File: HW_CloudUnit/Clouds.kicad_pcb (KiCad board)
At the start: 2 copper layers, 21.6 x 27 mm, 30 parts, among them J1 Conn_01x06, J2 Conn_01x03, J3 Conn_01x04, J4 Conn_01x04, U1 STM32G030F6Px, U2 AS5600L-ASOM, U3 DRV8313PWPR

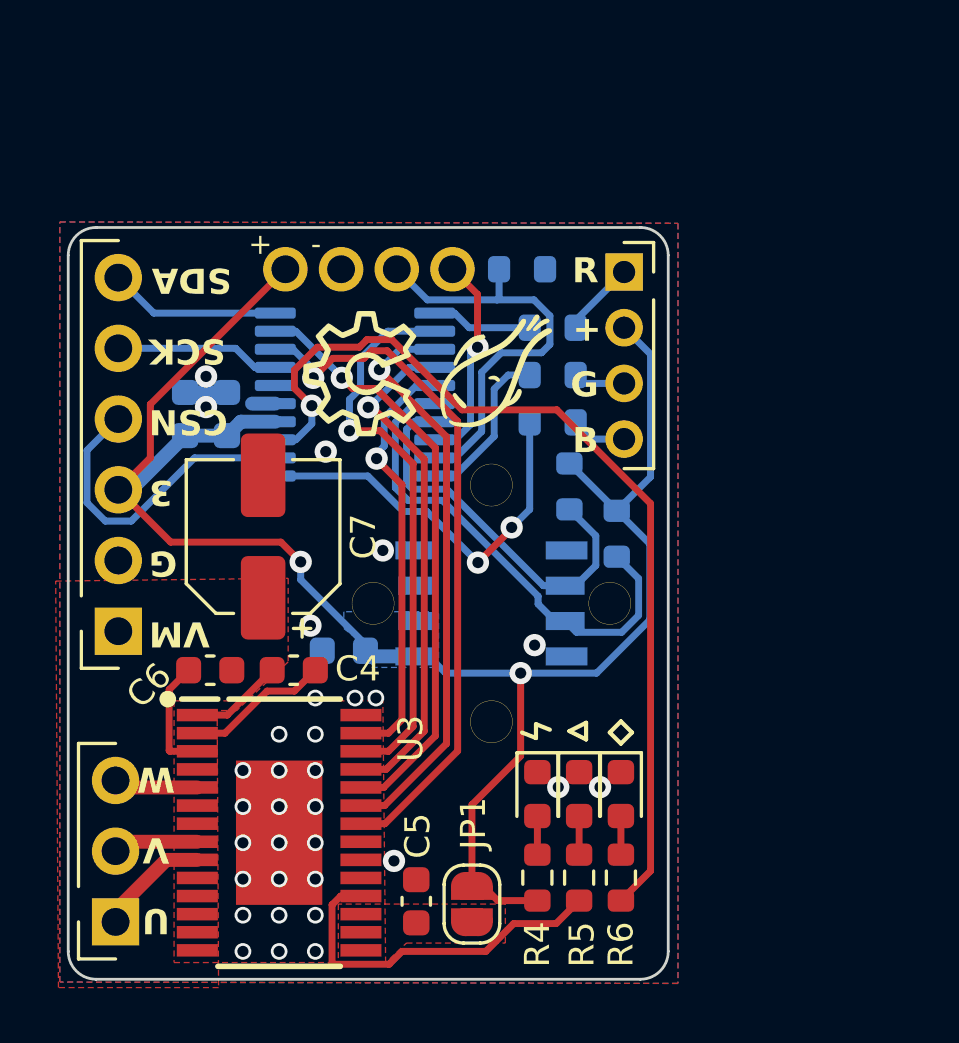
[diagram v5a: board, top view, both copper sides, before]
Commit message: Update clouds unit PCB with new motor dimensions
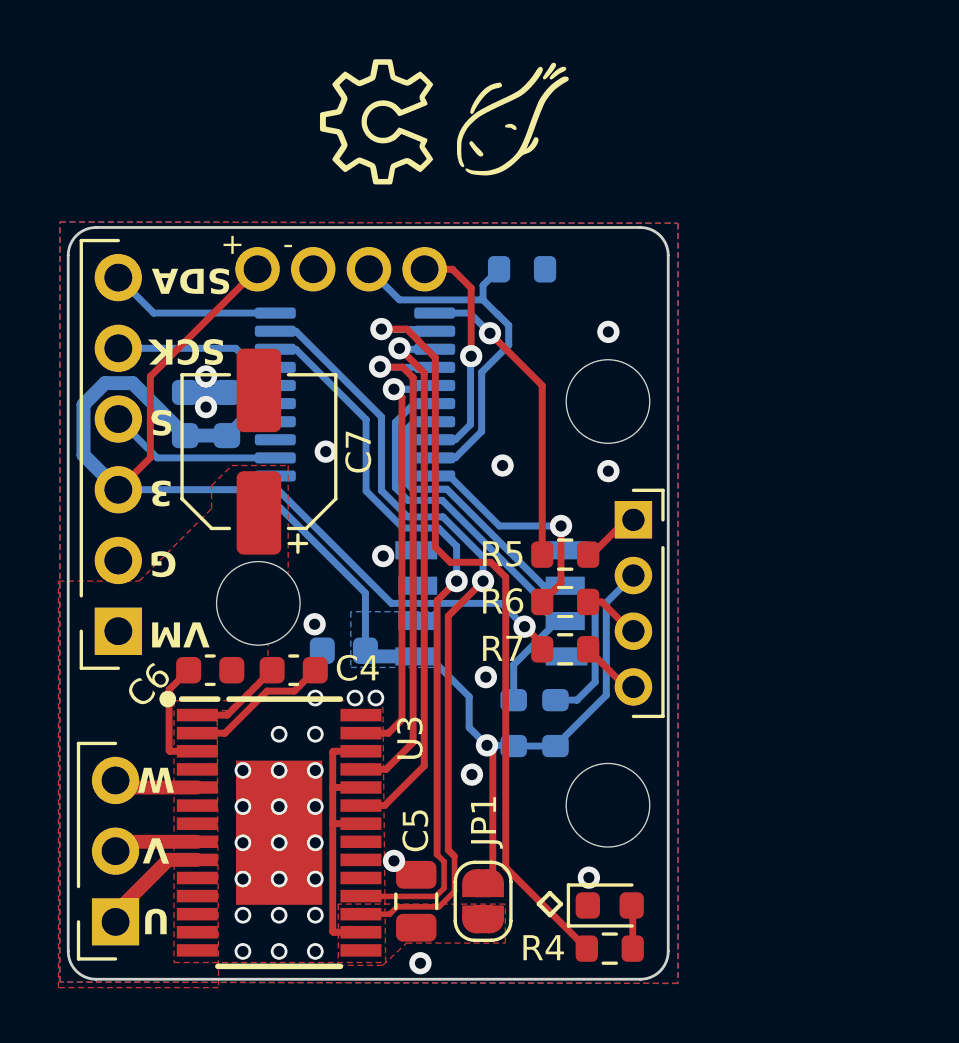
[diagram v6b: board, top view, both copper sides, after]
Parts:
- removed the D1 at (35.0, 38.5)
- removed D2: Green, LED_SMD:LED_0603_1608Metric
- removed the R4 at (35.0, 41.5)
- removed the R5 at (36.5, 41.5)
- C5: footprint Capacitor_SMD:C_0603_1608Metric -> Capacitor_SMD:C_0805_2012Metric
- H1: footprint Clouds_footprints:MountingHoles_M1.4_Diag8.5 -> Clouds_footprints:MountingHoles_M3_Tri14.5
- R5: renamed from R7; value TBD -> 220; moved to F.Cu
- R6: renamed from R8; value TBD -> 220; moved to F.Cu
- R7: renamed from R9; value TBD -> 220; moved to F.Cu
- moved G*** 9.06 mm to (34.2, 14.2)
- moved G*** 9.06 mm to (29.3, 14.4)
- moved J3 8.91 mm to (38.5, 28.7)
- moved R3 8.51 mm to (35.7, 36.0), turned to 90 degrees
- moved R7 8.16 mm to (36.0, 33.4)
- moved R5 8.16 mm to (36.0, 29.9)
- moved R6 8.16 mm to (36.0, 31.6)
- moved R2 7.74 mm to (34.2, 36.0), turned to 90 degrees
- moved D1 4.02 mm to (37.6, 42.5), turned to 0 degrees
- moved C7 3.05 mm to (25.1, 26.2)
- moved R4 2.58 mm to (37.6, 44.1), turned to 0 degrees
- moved J4 1.00 mm to (28.0, 19.7)
- moved JP1 0.41 mm to (33.1, 42.4)
- turned H1 to -30 degrees
- renumbered D3 to D1, R6 to R4
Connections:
- U1 pad 12: EN_W -> LED_ACT
- U1 pad 3: LED_ACT -> unconnected-(U1-PC15-Pad3)
- U1 pad 8: EN_U -> NFAULT
- U1 pad 9: EN_V -> NSLEEP
- U3 pad 17: V3P3O -> NSLEEP
- U3 pad 22: EN_U -> V3P3O
- U3 pad 24: EN_V -> V3P3O
- U3 pad 26: EN_W -> V3P3O
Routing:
- net NSLEEP: track 0.00 -> 28.7 mm, vias 0 -> 1
- net EN_U: track 25.0 -> 0.00 mm, vias 1 -> 0
- net EN_V: track 21.3 -> 0.00 mm, vias 1 -> 0
- net EN_W: track 20.3 -> 0.00 mm, vias 1 -> 0
- net NFAULT: track 13.1 -> 26.7 mm, vias 0 -> 1
- net V3P3O: track 0.00 -> 10.5 mm
- net +3.3V: track 65.1 -> 55.8 mm, vias 2 -> 1
- net LED_R: track 3.63 -> 11.0 mm, vias 0 -> 1
- net LED_ACT: track 34.1 -> 28.6 mm
- net UNIT_CSN: track 11.4 -> 6.22 mm
- net LED_G: track 5.91 -> 8.29 mm, vias 0 -> 1
- net MAG_SDA: track 14.6 -> 16.6 mm
- net SWCLK: track 15.4 -> 13.5 mm
- net LED_B: track 14.4 -> 12.5 mm, vias 2 -> 1
- net Net-(D2-A): track 1.39 -> 0.00 mm
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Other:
- board text added: "S"
- board text removed: "+"
- board text removed: "B"
- board text removed: "CSN"
- board text removed: "R"

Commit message: Further revise PCB design
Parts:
- moved G*** 12.3 mm to (33.8, 25.9)
- moved G*** 6.70 mm to (33.6, 20.9)
- moved C6 3.07 mm to (20.4, 35.0), turned to 180 degrees
- moved C4 2.85 mm to (23.4, 34.2)
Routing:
- net Net-(U3-CPH): track 5.18 -> 3.24 mm
- net Net-(U3-CPL): track 3.36 -> 1.58 mm
- net +3.3V: track 55.8 -> 54.6 mm
- net Net-(U3-VCP): track 4.20 -> 3.28 mm
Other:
- board text added: "23-WnSolst"
- board text added: "Rev. 4"
- board text removed: "*"
- board text removed: "23-Flurry"
- board text removed: "Rev. 3"

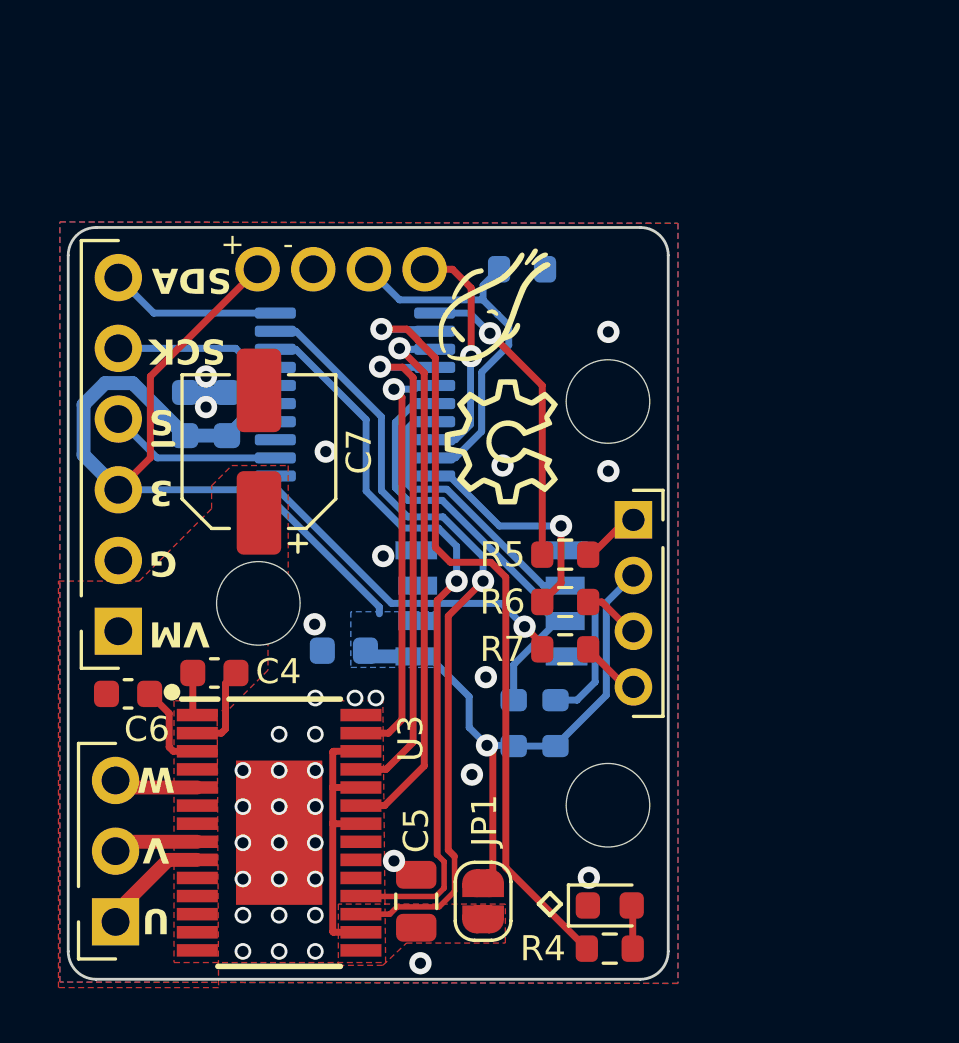
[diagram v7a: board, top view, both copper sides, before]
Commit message: Revise PCB and submit for fabrication (Rev. 4)
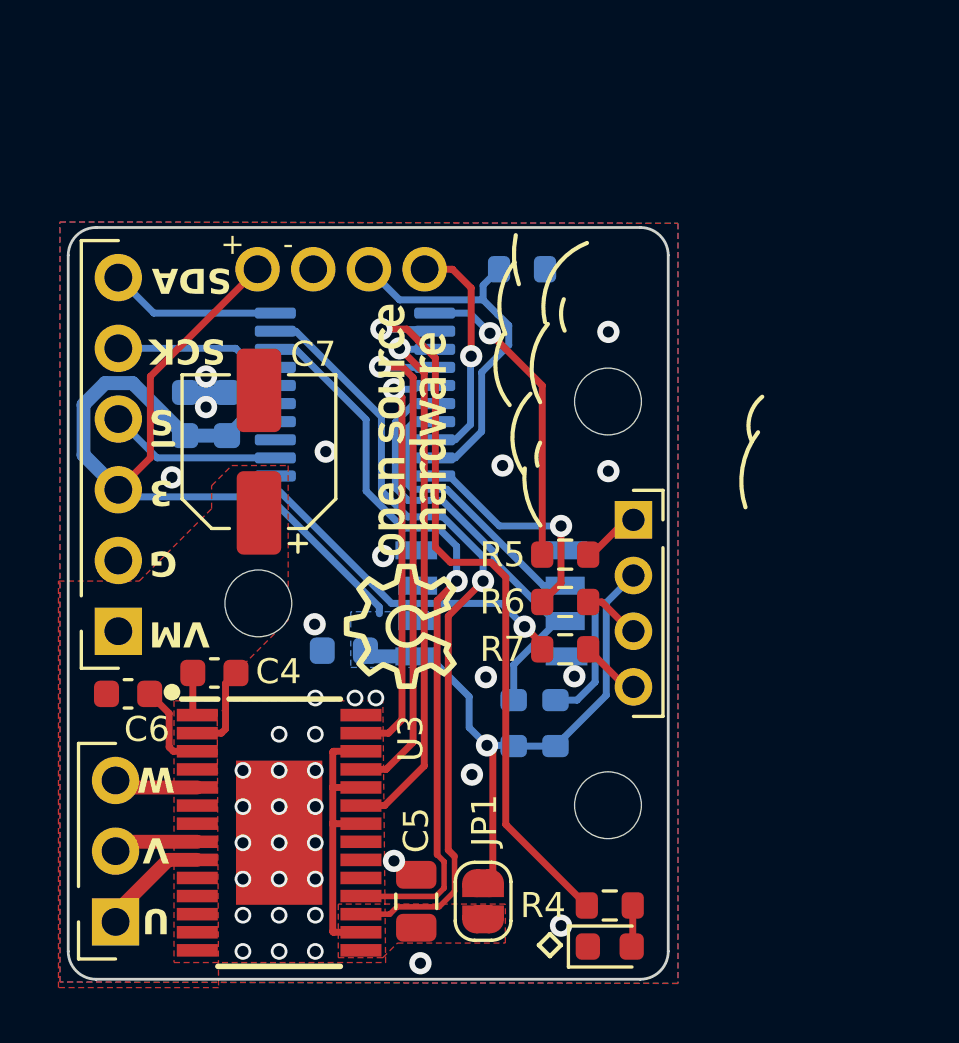
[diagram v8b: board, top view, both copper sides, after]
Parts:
- added G***: LOGO, LOGO, F.Cu at (30.4, 25.5)
- G***: moved to B.Cu
- moved G*** 20.9 mm to (34.4, 41.8), turned to -90 degrees
- moved G*** 7.55 mm to (30.1, 32.5)
- moved R4 1.55 mm to (37.6, 42.5)
- moved D1 1.48 mm to (37.6, 44.0)
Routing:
- net LED_ACT: track 28.6 -> 27.1 mm
- net GND: vias 36 -> 38
